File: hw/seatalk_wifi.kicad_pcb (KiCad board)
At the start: 2 copper layers, 31 x 22 mm, 41 parts, among them Q1 2n7002, Q2 BSS138, SW1 SW_SPST, SW2 SW_SPST, U1 AP62300_SOT23-6, U2 ESP-12E, U3 MAX3221_TSSOP16

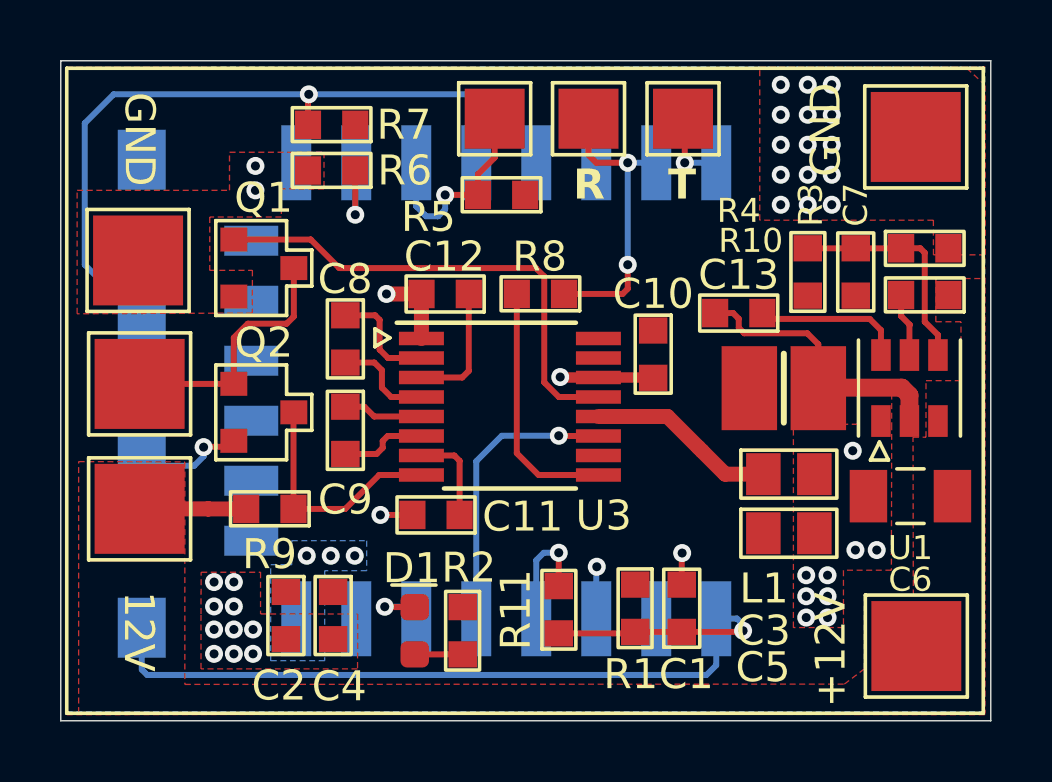
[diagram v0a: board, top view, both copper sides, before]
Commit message: Added R12 which allows an RS232 to WiFi bridge function.
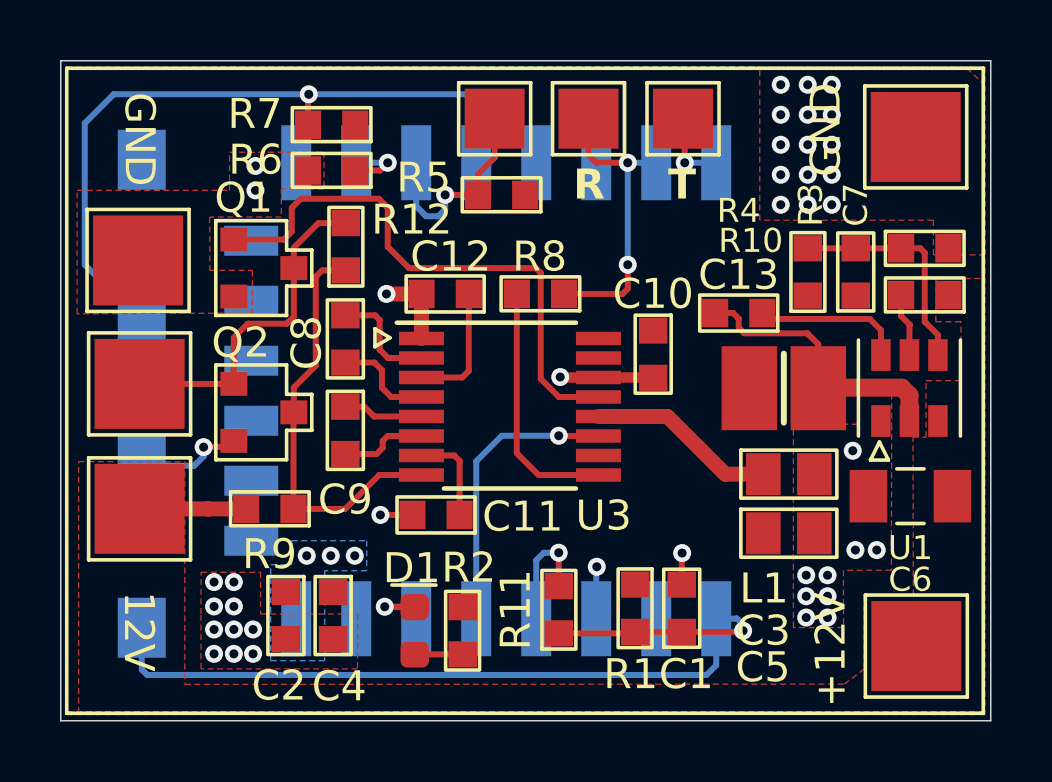
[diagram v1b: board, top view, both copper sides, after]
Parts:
- added R12: 0, resistor_SMD:R_0603_1608Metric, F.Cu at (132.5, 95.2)
- Q1: value 2n7002 -> 2N7002
- Q2: value BSS138 -> 2N7002
- R11: value 10K -> 1K
- R8: value 10K -> 3.3K
- U3: value MAX3221_TSSOP16 -> MAX3221CPWR
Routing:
- net /RXD: track 7.96 -> 13.9 mm
- net /SEATALK1: track 8.59 -> 11.3 mm
- net /TXD: track 16.4 -> 18.8 mm
- net /GPIO15: track 3.22 -> 2.24 mm
